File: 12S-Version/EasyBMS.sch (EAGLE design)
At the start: 156 parts, among them IC1 LM2596S-5.0_NOPB, IC2 LTC6811IG-1#PBF, Q10 BSS84LT1G, Q11 BSS84LT1G, Q12 BSS84LT1G, Q13 BSS84LT1G, Q2 BSS84LT1G, Q3 BSS84LT1G, Q4 BSS84LT1G, Q5 BSS84LT1G, Q6 BSS84LT1G, Q7 BSS84LT1G, Q8 BSS84LT1G, Q9 BSS84LT1G, T1 C8545

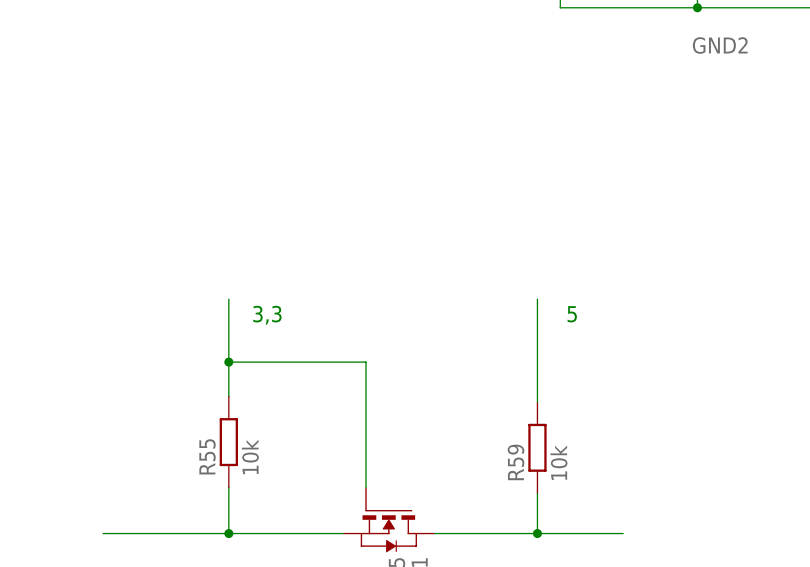
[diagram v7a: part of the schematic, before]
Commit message: paneled boards removed
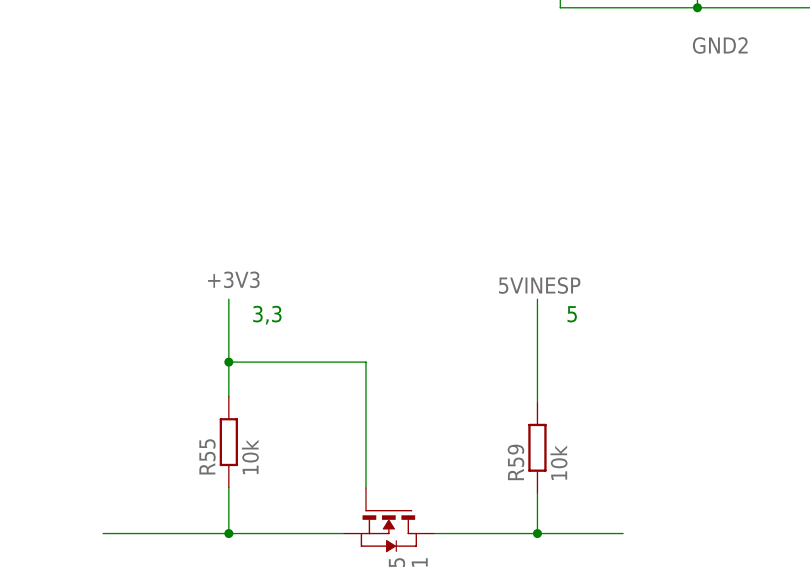
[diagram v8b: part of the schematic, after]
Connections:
- removed net N$18: R59.2
- removed net N$5: R55.2, T1.G
- net +3V3: now also R55.2, T1.G
- net 5VINESP: now also R59.2
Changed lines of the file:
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@@
 <label x="170.815" y="375.285" size="1.778" layer="95"/>
+</segment>
+<segment>
+<pinref part="R55" gate="G$1" pin="2"/>
+<wire x1="-5.08" y1="224.155" x2="-5.08" y2="227.965" width="0.1524" layer="91"/>
+<wire x1="-5.08" y1="227.965" x2="-5.08" y2="234.95" width="0.1524" layer="91"/>
+<pinref part="T1" gate="A" pin="G"/>
+<wire x1="10.16" y1="213.995" x2="10.16" y2="227.965" width="0.1524" layer="91"/>
+<wire x1="10.16" y1="227.965" x2="-5.08" y2="227.965" width="0.1524" layer="91"/>
+<junction x="-5.08" y="227.965"/>
+<label x="-7.62" y="236.22" size="1.778" layer="95"/>
 </segment>
 </net>
@@
 <wire x1="184.785" y1="356.87" x2="170.815" y2="356.87" width="0.1524" layer="91"/>
 <label x="170.815" y="356.87" size="1.778" layer="95"/>
+</segment>
+<segment>
+<pinref part="R59" gate="G$1" pin="2"/>
+<wire x1="29.21" y1="223.52" x2="29.21" y2="234.95" width="0.1524" layer="91"/>
+<label x="24.765" y="235.585" size="1.778" layer="95"/>
 </segment>
 </net>
@@
 </segment>
 </net>
-<net name="N$5" class="0">
-<segment>
-<pinref part="R55" gate="G$1" pin="2"/>
-<wire x1="-5.08" y1="224.155" x2="-5.08" y2="227.965" width="0.1524" layer="91"/>
-<wire x1="-5.08" y1="227.965" x2="-5.08" y2="234.95" width="0.1524" layer="91"/>
-<pinref part="T1" gate="A" pin="G"/>
-<wire x1="10.16" y1="213.995" x2="10.16" y2="227.965" width="0.1524" layer="91"/>
-<wire x1="10.16" y1="227.965" x2="-5.08" y2="227.965" width="0.1524" layer="91"/>
-<junction x="-5.08" y="227.965"/>
-</segment>
-</net>
 <net name="N$6" class="0">
 <segment>
@@
 </segment>
 </net>
-<net name="N$18" class="0">
-<segment>
-<pinref part="R59" gate="G$1" pin="2"/>
-<wire x1="29.21" y1="223.52" x2="29.21" y2="234.95" width="0.1524" layer="91"/>
-</segment>
-</net>
